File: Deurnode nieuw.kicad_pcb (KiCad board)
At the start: 2 copper layers, 221.3 x 60.3 mm, 37 parts, among them J1 EXT1, J10 Jumper Output, J11 Jumper Rel./Fet, J12 Screw_Terminal_01x03, J13 Screw_Terminal_01x03, J14 Screw_Terminal_01x02, J15 Screw_Terminal_01x02, J16 Conn_01x02, J17 Conn_01x02, J2 EXT2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

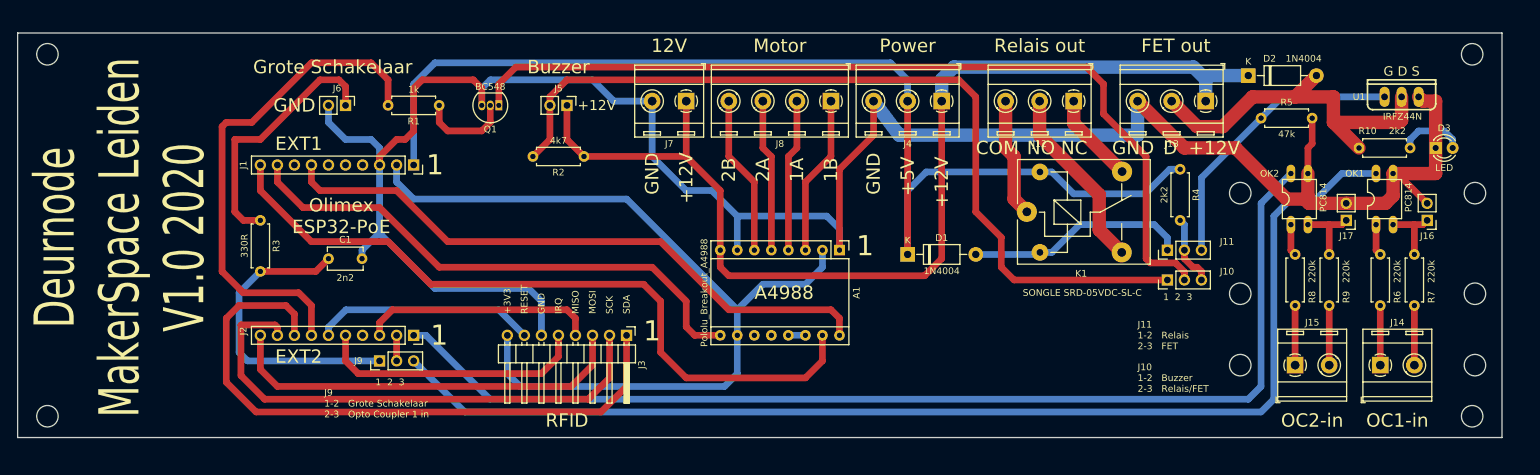
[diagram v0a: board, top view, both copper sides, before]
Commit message: DC-DC converter 12V -> 5V added to concept version 0.3
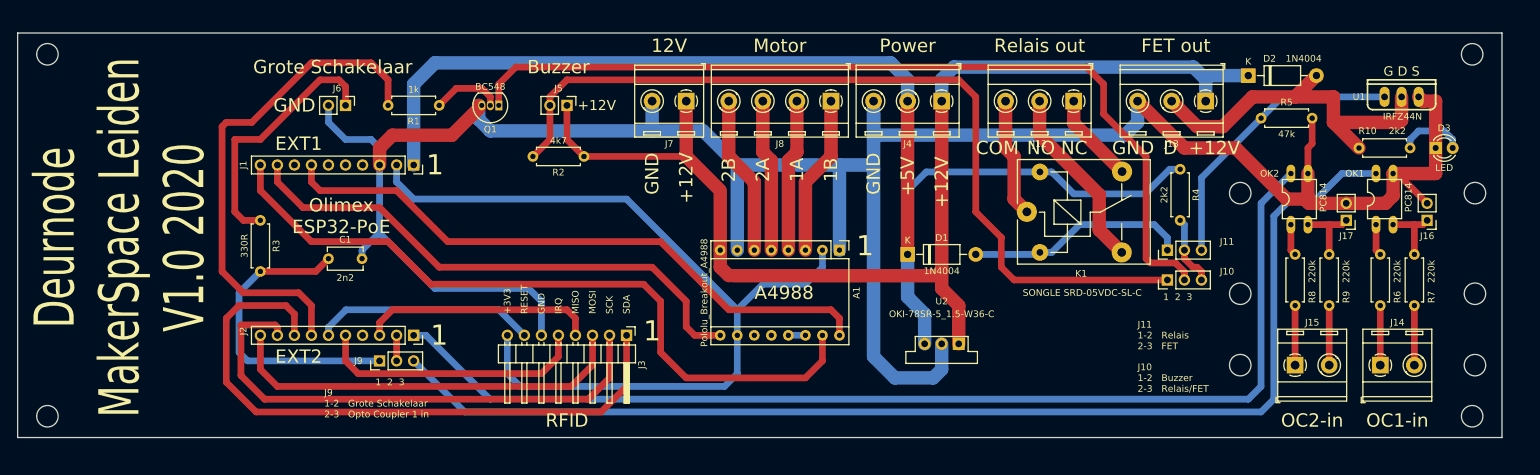
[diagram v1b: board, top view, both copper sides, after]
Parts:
- added U2: OKI-78SR-5_1.5-W36-C, Converter_DCDC:Converter_DCDC_muRata_OKI-78SR_Vertical, F.Cu at (177.8, 117.5)
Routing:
- net GND: track 328.4 -> 365.8 mm
- net +5V: track 168.6 -> 183.0 mm
- net +12V: track 162.8 -> 175.8 mm
- net Net-(Q1-Pad2): track 13.8 -> 10.5 mm

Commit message: README.md and other docs added, additional 12V connector added to design concept version 0.4
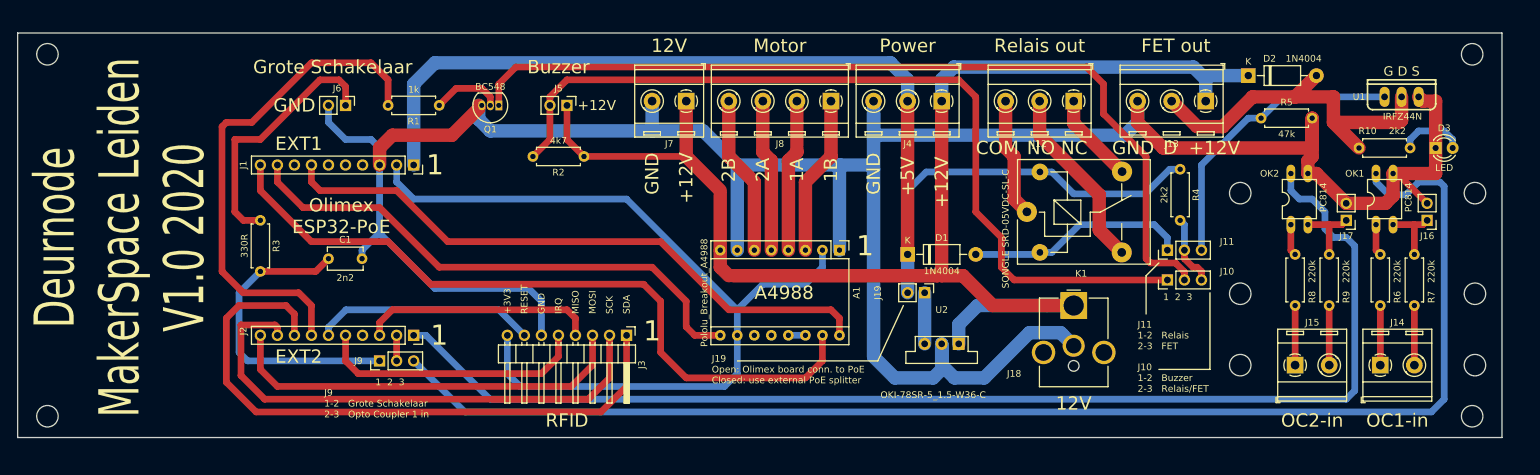
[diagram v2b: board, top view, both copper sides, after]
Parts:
- added J18: Barrel_Jack, Connector_BarrelJack:BarrelJack_CUI_PJ-063AH_Horizontal_CircularHoles, F.Cu at (194.9, 111.8)
- added J19: Conn_01x02, Connector_PinHeader_2.54mm:PinHeader_1x02_P2.54mm_Vertical, F.Cu at (172.7, 109.9)
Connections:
- U2 pad 3: +5V -> Net-(J19-Pad1)
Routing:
- net GND: track 365.8 -> 397.6 mm
- net +12V: track 175.8 -> 207.3 mm
- net Net-(J9-Pad3): track 177.4 -> 202.6 mm
- net GPI39: track 164.7 -> 183.4 mm
- net +5V: track 183.0 -> 174.3 mm
- net Net-(J19-Pad1): track 0.00 -> 7.62 mm
- net Net-(J11-Pad3): track 43.1 -> 44.2 mm
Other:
- board text added: "J19 Open: Olimex board conn. to PoE Closed: use external PoE splitter"

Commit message: By means of two jumpers the FET components are isolated from the rest of the board. Current concept version 0.5
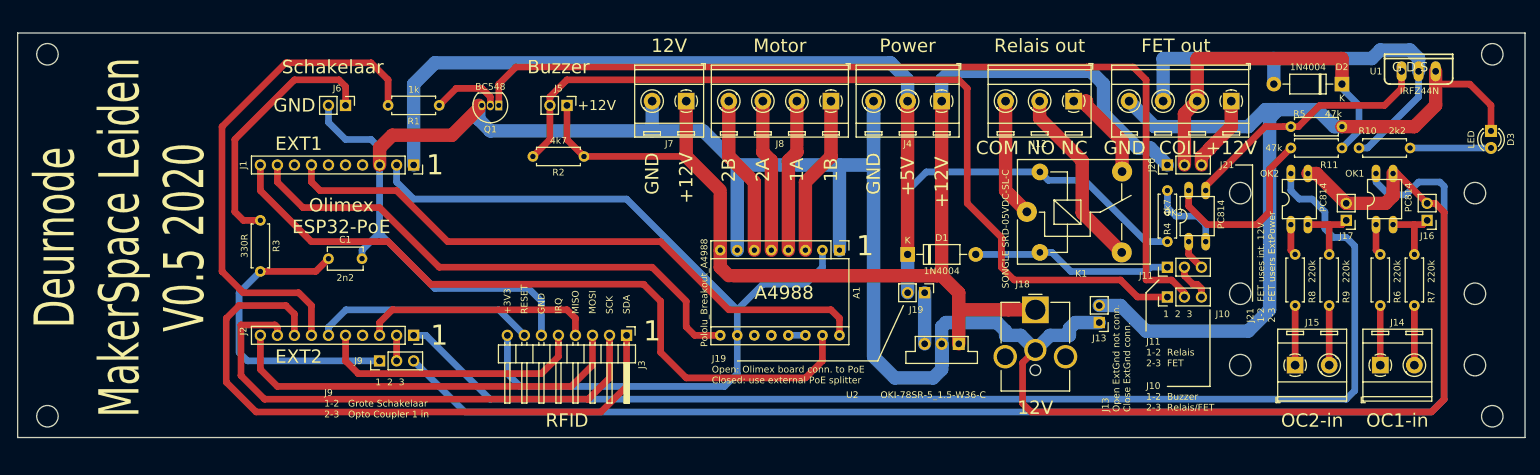
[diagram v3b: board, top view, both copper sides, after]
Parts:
- added J20: Jumper 1 External Power, Connector_PinHeader_2.54mm:PinHeader_1x03_P2.54mm_Vertical, F.Cu at (208.9, 90.8)
- added J21: Screw_Terminal_01x04, TerminalBlock_RND:TerminalBlock_RND_205-00289_1x04_P5.08mm_Horizontal, F.Cu at (218.4, 81.3)
- added OK3: PC814, PC814:DIL04, F.Cu at (213.4, 98.4)
- added R11: 47k, Resistor_THT:R_Axial_DIN0207_L6.3mm_D2.5mm_P7.62mm_Horizontal, F.Cu at (234.9, 88.3)
- J13: value Screw_Terminal_01x03 -> Jumper 2 External Power; footprint TerminalBlock_RND:TerminalBlock_RND_205-00288_1x03_P5.08mm_Horizontal -> Connector_PinHeader_2.54mm:PinHeader_1x02_P2.54mm_Vertical
- R4: value 2k2 -> 4k7
- moved J13 36.6 mm to (198.8, 114.3)
- moved D2 14.0 mm to (234.9, 78.7), turned to 180 degrees
- moved R4 11.0 mm to (208.9, 102.2), turned to 90 degrees
- moved D3 8.64 mm to (257.2, 85.7), turned to 270 degrees
- moved J18 5.75 mm to (189.2, 112.4)
- moved R5 4.62 mm to (227.3, 85.1)
- moved U1 4.58 mm to (246.4, 76.8)
- moved J11 2.54 mm to (208.9, 106.0)
- moved J10 2.54 mm to (208.9, 110.5)
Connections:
- A1 pad 11: Net-(A1-Pad11) -> (no net)
- A1 pad 12: Net-(A1-Pad12) -> (no net)
- D2 pad 1: +12V -> Net-(D2-Pad1)
- D3 pad 1: GND -> Net-(D3-Pad1)
- J1 pad 4: ESP_EN -> (no net)
- J1 pad 5: GPIO0 -> (no net)
- J1 pad 6: GPIO1_U0TXD -> (no net)
- J1 pad 8: GPIO3_U0RXD -> (no net)
- J13 pad 1: +12V -> GND
- J13 pad 2: Net-(D2-Pad2) -> Net-(D3-Pad1)
- J2 pad 4: GPI34_BUT1 -> (no net)
- R4 pad 2: Net-(J10-Pad3) -> Net-(OK3-Pad2)
- R5 pad 1: Net-(J11-Pad3) -> Net-(OK3-Pad3)
- R5 pad 2: GND -> Net-(D3-Pad1)
- U1 pad 1: Net-(J11-Pad3) -> Net-(OK3-Pad3)
- U1 pad 3: GND -> Net-(D3-Pad1)
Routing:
- net Net-(D3-Pad1): track 0.00 -> 127.8 mm
- net Net-(D2-Pad1): track 0.00 -> 53.7 mm
- net Net-(J11-Pad3): track 44.2 -> 4.60 mm
- net Net-(OK3-Pad3): track 0.00 -> 38.4 mm
- net +12V: track 207.3 -> 179.0 mm
- net Net-(OK3-Pad4): track 0.00 -> 27.2 mm
- net Net-(D2-Pad2): track 55.0 -> 67.1 mm
- net Net-(OK3-Pad2): track 0.00 -> 11.8 mm
- net Net-(J20-Pad3): track 0.00 -> 11.4 mm
- net Net-(J10-Pad2): track 132.5 -> 139.2 mm
- net Net-(J10-Pad3): track 10.6 -> 5.87 mm
- net GND: track 397.6 -> 400.8 mm
- net Net-(D1-Pad2): track 33.1 -> 30.1 mm
- net Net-(D3-Pad2): track 9.94 -> 12.1 mm
- net Net-(J12-Pad1): track 13.5 -> 14.6 mm
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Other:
- board size 221.3 x 60.3 mm -> 224.8 x 60.3 mm
- board text added: "COIL"
- board text added: "Deurnode MakerSpace Leiden V0.5 2020"
- board text added: "J13 Open ExtGnd not conn. Close ExtGnd conn."
- board text added: "J21 1-2 FET uses int. 12V 2-3 FET users ExtPower"
- board text added: "Schakelaar"
- board text removed: "D"
- board text removed: "Deurnode MakerSpace Leiden V1.0 2020"
- board text removed: "Grote Schakelaar"

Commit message: Jumper added for Relais/FET override + correct footprint made for 12V barel jack current version concept V0.6
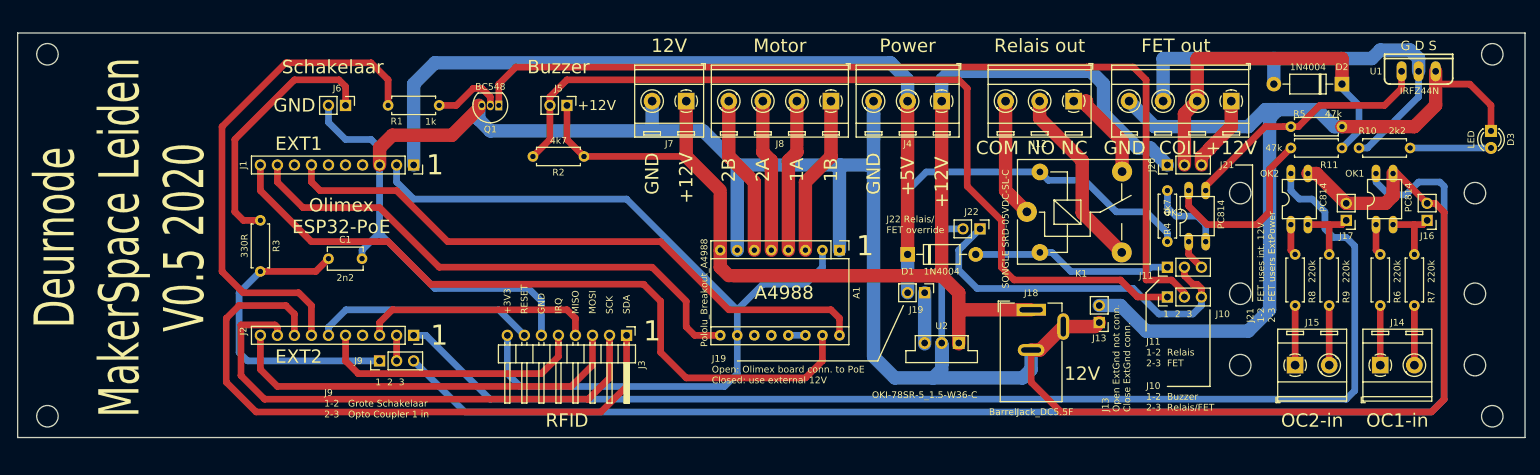
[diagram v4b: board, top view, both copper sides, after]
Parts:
- added J22: Jumper Rel./FET Override, Connector_PinHeader_2.54mm:PinHeader_1x02_P2.54mm_Vertical, F.Cu at (181.0, 100.3)
- J13: value Jumper 2 External Power -> Jumper 2 External FET Power
- J18: value Barrel_Jack -> BarrelJack_DC5.5F; footprint Connector_BarrelJack:BarrelJack_CUI_PJ-063AH_Horizontal_CircularHoles -> Footprints:BarrelJack_DC5.5F
- J19: value Conn_01x02 -> Jumper Use external 12V
- J20: value Jumper 1 External Power -> Jumper 1 External FET Power
- moved J18 0.63 mm to (188.6, 112.4)
- moved U2 0.12 mm to (177.8, 117.3)
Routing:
- net Net-(J10-Pad3): track 5.87 -> 53.1 mm
- net GND: track 400.8 -> 415.5 mm
- net +5V: track 173.8 -> 174.6 mm
- net +12V: track 179.0 -> 178.4 mm
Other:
- board text added: "J19 Open: Olimex board conn. to PoE Closed: use external 12V"
- board text added: "J22 Relais/ FET override"
- board text removed: "J19 Open: Olimex board conn. to PoE Closed: use external PoE splitter"

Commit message: removed a lot of jumpers, replaced connectors, added groundplane etc.
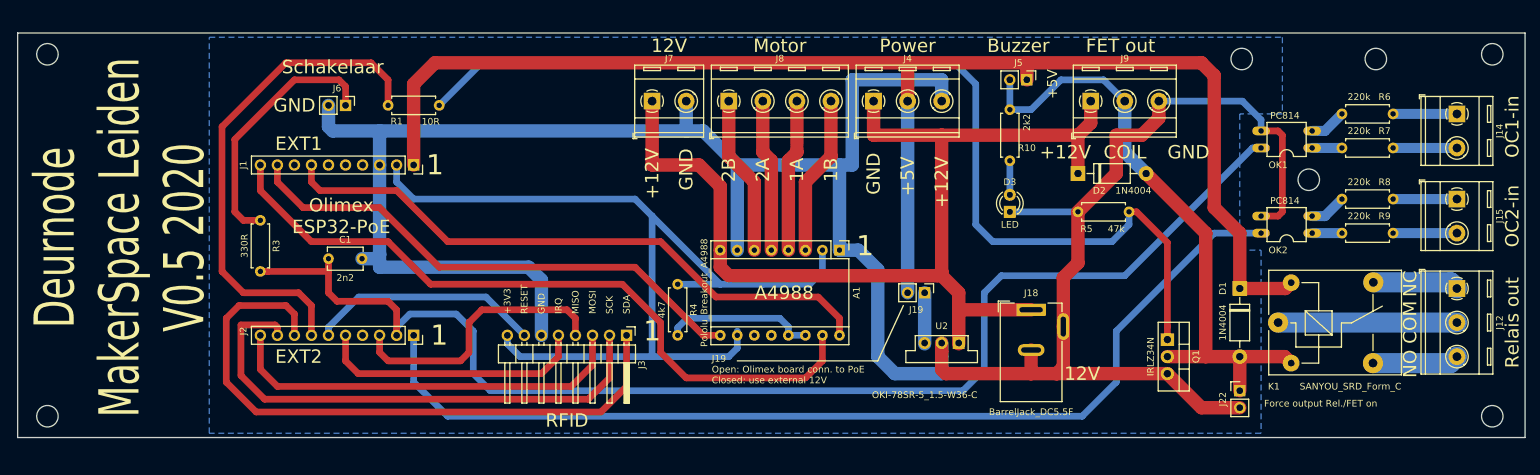
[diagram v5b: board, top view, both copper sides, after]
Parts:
- removed J10: Jumper Output, Connector_PinHeader_2.54mm:PinHeader_1x03_P2.54mm_Vertical
- removed J11: Jumper Rel./Fet, Connector_PinHeader_2.54mm:PinHeader_1x03_P2.54mm_Vertical
- removed J13: Jumper 2 External FET Power, Connector_PinHeader_2.54mm:PinHeader_1x02_P2.54mm_Vertical
- removed J16, J17: Conn_01x02, Connector_PinHeader_2.54mm:PinHeader_1x02_P2.54mm_Vertical
- removed J20: Jumper 1 External FET Power, Connector_PinHeader_2.54mm:PinHeader_1x03_P2.54mm_Vertical
- removed J21: Screw_Terminal_01x04, TerminalBlock_RND:TerminalBlock_RND_205-00289_1x04_P5.08mm_Horizontal
- removed OK3: PC814, PC814:DIL04
- removed R11: 47k, Resistor_THT:R_Axial_DIN0207_L6.3mm_D2.5mm_P7.62mm_Horizontal
- removed R2: 4k7, Resistor_THT:R_Axial_DIN0207_L6.3mm_D2.5mm_P7.62mm_Horizontal
- removed U1: IRFZ44N, IRFZ44N:TO-220
- J22: value Jumper Rel./FET Override -> Force output Rel./FET on
- J9: value Jumper Input -> Screw_Terminal_01x03; footprint Connector_PinHeader_2.54mm:PinHeader_1x03_P2.54mm_Vertical -> TerminalBlock_RND:TerminalBlock_RND_205-00288_1x03_P5.08mm_Horizontal
- K1: value SONGLE SRD-05VDC-SL-C -> SANYOU_SRD_Form_C
- Q1: value BC548 -> IRLZ34N; footprint Package_TO_SOT_THT:TO-92_Inline -> Package_TO_SOT_THT:TO-220-3_Vertical
- R1: value 1k -> 10R
- moved J9 112.9 mm to (197.5, 81.3), turned to 0 degrees
- moved Q1 105.6 mm to (208.9, 116.8), turned to 270 degrees
- moved R4 73.3 mm to (135.9, 108.6), turned to 270 degrees
- moved D3 72.8 mm to (185.4, 97.8), turned to 90 degrees
- moved J5 68.7 mm to (188.0, 78.1)
- moved J12 63.6 mm to (252.1, 109.2), turned to 270 degrees
- moved R10 52.4 mm to (185.4, 82.5), turned to 270 degrees
- moved D1 49.8 mm to (219.7, 109.2), turned to 270 degrees
- moved J22 45.6 mm to (219.7, 124.5), turned to 0 degrees
- moved D2 41.6 mm to (195.6, 92.1), turned to 0 degrees
- moved K1 40.9 mm to (225.4, 114.3)
- moved J14 39.2 mm to (252.1, 83.2), turned to 270 degrees
- moved J15 34.6 mm to (252.1, 95.9), turned to 270 degrees
- moved R6 28.6 mm to (242.6, 83.2), turned to 180 degrees
- moved R5 27.3 mm to (203.2, 97.8), turned to 180 degrees
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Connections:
- C1 pad 1: Net-(C1-Pad1) -> GPI36_U1RXD
- D2 pad 1: Net-(D2-Pad1) -> +12V
- D2 pad 2: Net-(D2-Pad2) -> Net-(D1-Pad2)
- D3 pad 1: Net-(D3-Pad1) -> GND
- J22 pad 1: Net-(J10-Pad3) -> Net-(D1-Pad2)
- J5 pad 1: +12V -> +5V
- J5 pad 2: Net-(J10-Pad1) -> Net-(D1-Pad2)
- J8 pad 1: Net-(A1-Pad3) -> Net-(A1-Pad6)
- J8 pad 2: Net-(A1-Pad4) -> Net-(A1-Pad5)
- J8 pad 3: Net-(A1-Pad5) -> Net-(A1-Pad4)
- J8 pad 4: Net-(A1-Pad6) -> Net-(A1-Pad3)
- J9 pad 1: Net-(C1-Pad1) -> +12V
- J9 pad 2: GPI36_U1RXD -> Net-(D1-Pad2)
- J9 pad 3: Net-(J9-Pad3) -> GND
- K1 pad 1: Net-(J12-Pad3) -> Net-(J12-Pad2)
- K1 pad 3: Net-(J12-Pad2) -> Net-(J12-Pad3)
- OK1 pad 2: Net-(J16-Pad1) -> Net-(OK1-Pad2)
- OK1 pad 4: Net-(J9-Pad3) -> GPI36_U1RXD
- OK2 pad 2: Net-(J17-Pad1) -> Net-(OK2-Pad2)
- Q1 pad 1: Net-(J10-Pad2) -> Net-(Q1-Pad1)
- Q1 pad 2: Net-(Q1-Pad2) -> Net-(D1-Pad2)
- R1 pad 1: Net-(Q1-Pad2) -> Net-(Q1-Pad1)
- R10 pad 1: Net-(D2-Pad2) -> Net-(D1-Pad2)
- R3 pad 2: Net-(C1-Pad1) -> GPI36_U1RXD
- R4 pad 1: +5V -> 3V3
- R4 pad 2: Net-(OK3-Pad2) -> Net-(A1-Pad13)
- R5 pad 1: Net-(OK3-Pad3) -> Net-(Q1-Pad1)
- R5 pad 2: Net-(D3-Pad1) -> GND
- R6 pad 2: Net-(OK1-Pad1) -> Net-(OK1-Pad2)
- R7 pad 2: Net-(J16-Pad1) -> Net-(OK1-Pad1)
- R8 pad 2: Net-(OK2-Pad1) -> Net-(OK2-Pad2)
- R9 pad 2: Net-(J17-Pad1) -> Net-(OK2-Pad1)
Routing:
- net Net-(J9-Pad3): track 202.6 -> 0.00 mm
- net GPI36_U1RXD: track 3.81 -> 191.3 mm
- net Net-(Q1-Pad1): track 0.00 -> 153.9 mm
- net Net-(J10-Pad2): track 139.2 -> 0.00 mm
- net Net-(J10-Pad1): track 129.1 -> 0.00 mm
- net Net-(D3-Pad1): track 127.8 -> 0.00 mm
- net Net-(D2-Pad2): track 67.1 -> 0.00 mm
- net Net-(D1-Pad2): track 30.1 -> 91.8 mm
- net Net-(D2-Pad1): track 53.7 -> 0.00 mm
- net Net-(J10-Pad3): track 53.1 -> 0.00 mm
- net Net-(C1-Pad1): track 45.8 -> 0.00 mm
- net Net-(OK3-Pad3): track 38.4 -> 0.00 mm
- net +5V: track 174.6 -> 211.7 mm
- net GPI39: track 183.4 -> 151.2 mm
- net GND: track 415.5 -> 384.2 mm
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- added copper zone on B.Cu, net GND
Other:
- outline, holes or cut-outs redrawn
- board text removed: "1 2 3"
- board text removed: "G D S"
- board text removed: "J10 1-2 Buzzer 2-3 Relais/FET"
- board text removed: "J11 1-2 Relais 2-3 FET"
- board text removed: "J13 Open ExtGnd not conn. Close ExtGnd conn."
- board text removed: "J21 1-2 FET uses int. 12V 2-3 FET users ExtPower"
- board text removed: "J22 Relais/ FET override"
- board text removed: "J9 1-2 Grote Schakelaar 2-3 Opto Coupler 1 in"

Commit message: Relais and FET are controlled separately, buzzer resistor added. Current version Concep V0.8
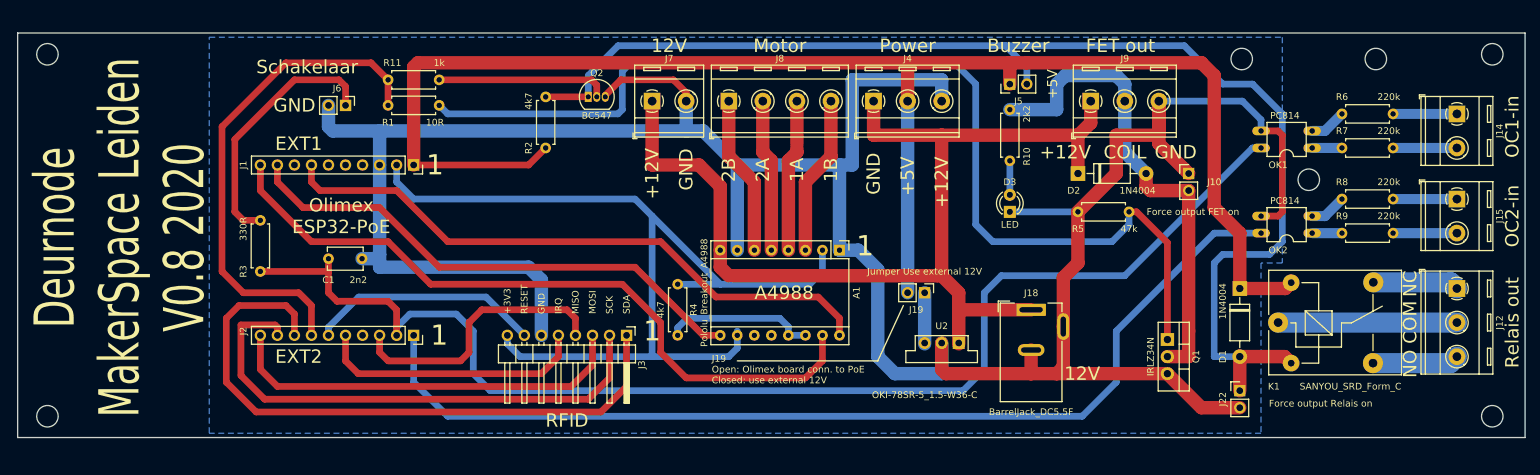
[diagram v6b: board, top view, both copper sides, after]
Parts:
- added J10: Force output FET on, Connector_PinHeader_2.54mm:PinHeader_1x02_P2.54mm_Vertical, F.Cu at (212.1, 92.1)
- added Q2: BC547, Package_TO_SOT_THT:TO-92_Inline, F.Cu at (122.6, 80.6)
- added R11: 1k, Resistor_THT:R_Axial_DIN0207_L6.3mm_D2.5mm_P7.62mm_Horizontal, F.Cu at (100.3, 78.1)
- added R2: 4k7, Resistor_THT:R_Axial_DIN0207_L6.3mm_D2.5mm_P7.62mm_Horizontal, F.Cu at (116.2, 88.3)
- J22: value Force output Rel./FET on -> Force output Relais on
- moved J5 2.62 mm to (185.4, 78.7), turned to 90 degrees
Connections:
- D2 pad 2: Net-(D1-Pad2) -> Net-(D2-Pad2)
- J9 pad 2: Net-(D1-Pad2) -> Net-(D2-Pad2)
- Q1 pad 2: Net-(D1-Pad2) -> Net-(D2-Pad2)
- R10 pad 1: Net-(D1-Pad2) -> Net-(D2-Pad2)
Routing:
- net Net-(D1-Pad2): track 91.8 -> 188.2 mm
- net Net-(D2-Pad2): track 0.00 -> 73.1 mm
- net GND: track 384.2 -> 413.6 mm
- net Net-(Q2-Pad2): track 0.00 -> 25.6 mm
- net +5V: track 211.7 -> 234.6 mm
- net Net-(Q1-Pad1): track 153.9 -> 158.3 mm
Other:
- board text added: "Deurnode MakerSpace Leiden V0.8 2020"
- board text removed: "Deurnode MakerSpace Leiden V0.5 2020"
